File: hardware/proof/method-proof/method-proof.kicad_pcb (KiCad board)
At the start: 4 copper layers, 40 x 30 mm, 21 parts, among them J1 5V_IN, J2 OUT, J3 PA1, U1 MCP1700T-3302E/TT, U2 MSPS003F4SPW20R

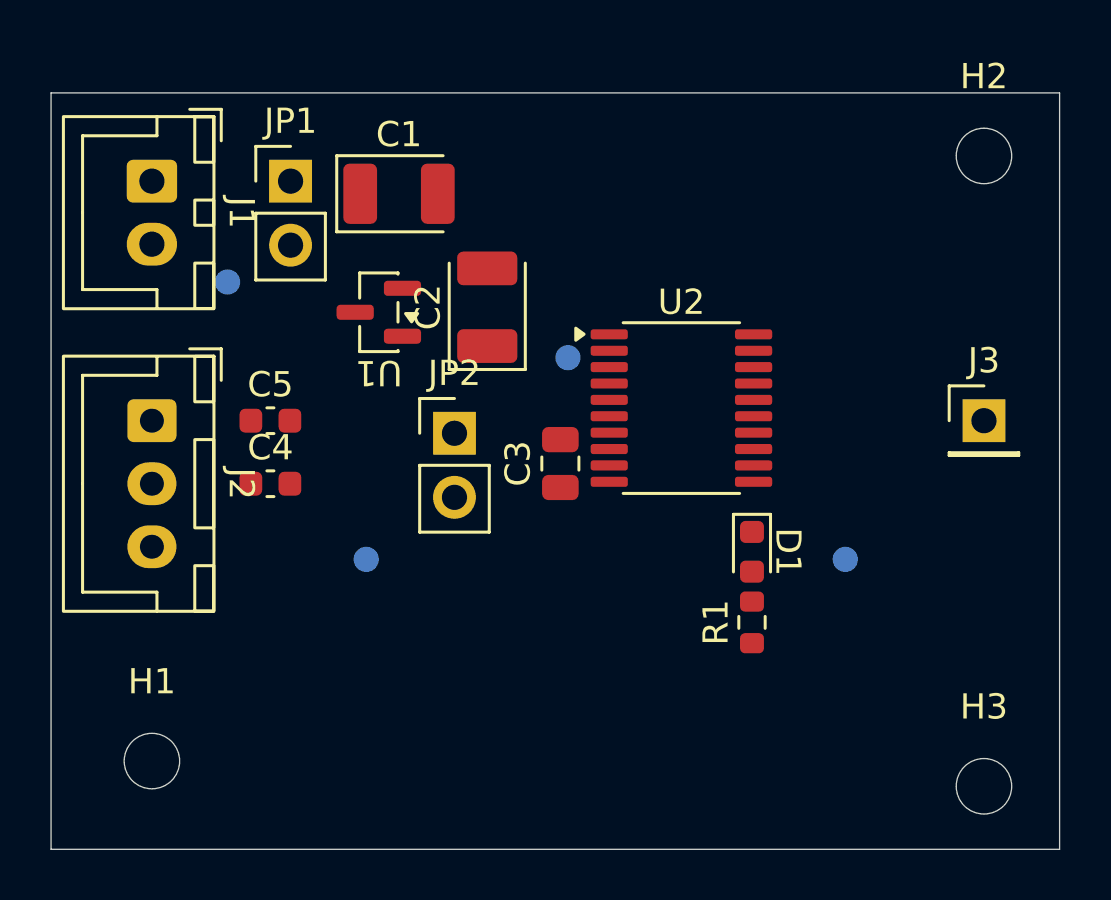
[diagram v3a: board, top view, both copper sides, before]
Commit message: hardware(method-proof): placement candidate 3: candidate 1 with the controller and the LED stage moved down four millimetres and the PA1 header with them
Not for manufacture.

Co-Authored-By: Claude Sonnet 5.5 <noreply@anthropic.com>
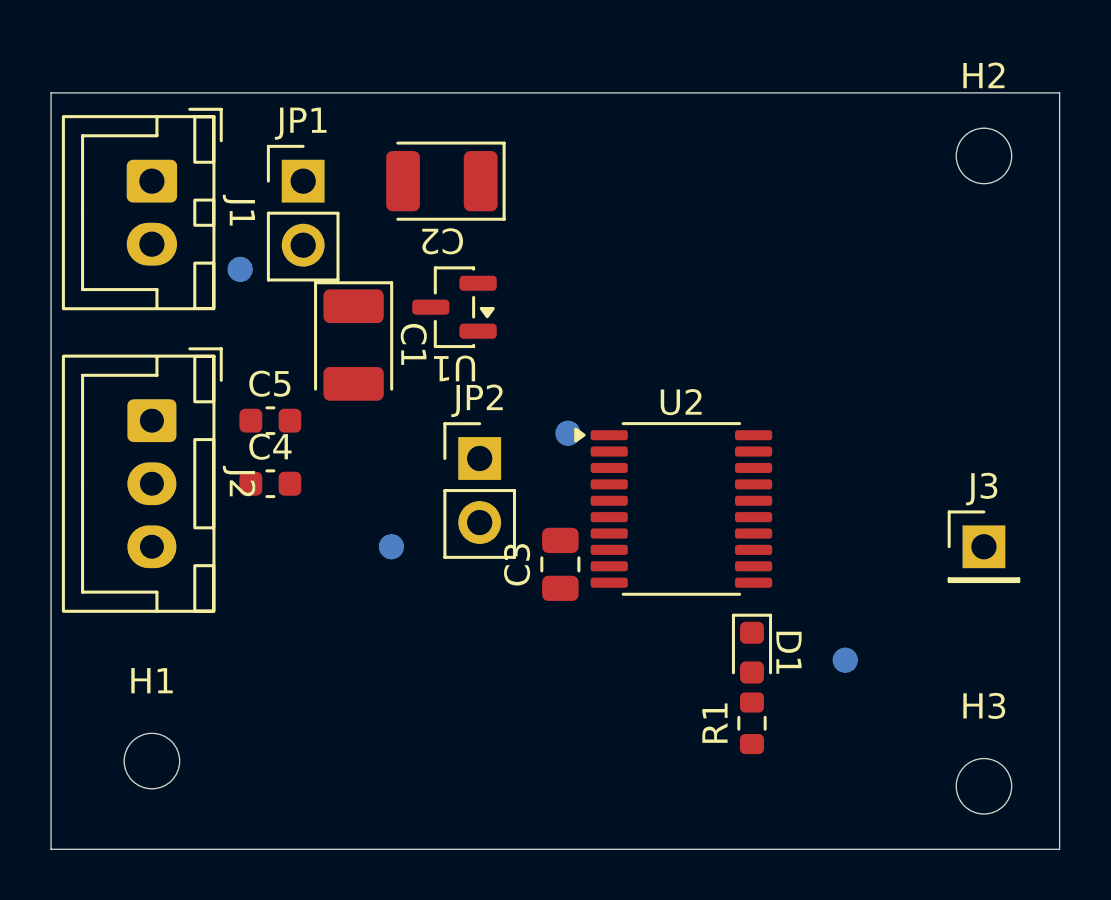
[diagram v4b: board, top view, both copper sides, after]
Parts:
- moved C1 6.26 mm to (112.0, 110.0), turned to -90 degrees
- moved C2 5.31 mm to (115.5, 103.5), turned to 180 degrees
- moved J3 5.00 mm to (137.0, 118.0)
- moved C3 4.00 mm to (120.2, 118.7)
- moved D1 4.00 mm to (127.8, 122.2)
- moved R1 4.00 mm to (127.8, 125.0)
- moved TP4 4.00 mm to (131.5, 122.5)
- moved U2 4.00 mm to (125.0, 116.5)
- moved U1 3.01 mm to (116.0, 108.5)
- moved TP3 3.00 mm to (120.5, 113.5)
- moved JP2 1.41 mm to (117.0, 114.5)
- moved TP2 1.12 mm to (113.5, 118.0)
- moved TP1 0.71 mm to (107.5, 107.0)
- moved JP1 0.50 mm to (110.0, 103.5)
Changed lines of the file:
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@@
 	(footprint "Connector_PinHeader_2.54mm:PinHeader_1x01_P2.54mm_Vertical"
 		(layer "F.Cu")
-		(at 137 113)
+		(at 137 118)
 		(property "Reference" "J3"
 			(at 0 -2.38 0)
@@
 	(footprint "Package_SO:TSSOP-20_4.4x6.5mm_P0.65mm"
 		(layer "F.Cu")
-		(at 125 112.5)
+		(at 125 116.5)
 		(property "Reference" "U2"
 			(at 0 -4.2 0)
@@
 	(footprint "Connector_PinHeader_2.54mm:PinHeader_1x02_P2.54mm_Vertical"
 		(layer "F.Cu")
-		(at 109.5 103.5)
+		(at 110 103.5)
 		(property "Reference" "JP1"
 			(at 0 -2.38 0)
@@
 	(footprint "Resistor_SMD:R_0603_1608Metric"
 		(layer "F.Cu")
-		(at 127.8 121 90)
+		(at 127.8 125 90)
 		(property "Reference" "R1"
 			(at 0 -1.43 90)
@@
 	(footprint "Capacitor_Tantalum_SMD:CP_EIA-3528-21_Kemet-B"
 		(layer "F.Cu")
-		(at 113.8 104)
+		(at 112 110 -90)
 		(property "Reference" "C1"
-			(at 0 -2.35 0)
+			(at 0 -2.35 270)
 			(unlocked yes)
 			(layer "F.SilkS")
@@
 		)
 		(property "Value" "47uF"
-			(at 0 2.35 0)
+			(at 0 2.35 270)
 			(unlocked yes)
 			(layer "F.SilkS")
@@
 		)
 		(property "Datasheet" ""
-			(at 0 0 0)
+			(at 0 0 270)
 			(layer "F.Fab")
 			(hide yes)
@@
 		)
 		(property "Description" ""
-			(at 0 0 0)
+			(at 0 0 270)
 			(layer "F.Fab")
 			(hide yes)
@@
 		(duplicate_pad_numbers_are_jumpers no)
 		(fp_line
-			(start -2.470001 -1.510001)
-			(end -2.470001 1.51)
+			(start -2.470001 1.51)
+			(end 1.75 1.51)
 			(stroke
 				(width 0.12)
@@
 		)
 		(fp_line
-			(start -2.470001 1.51)
-			(end 1.75 1.51)
+			(start -2.470001 -1.510001)
+			(end -2.470001 1.51)
 			(stroke
 				(width 0.12)
@@
 		)
 		(fp_line
-			(start -1.75 -0.7)
-			(end -1.75 1.4)
+			(start -1.75 1.4)
+			(end 1.75 1.4)
 			(stroke
 				(width 0.1)
@@
 		)
 		(fp_line
-			(start -1.75 1.4)
-			(end 1.75 1.4)
+			(start 1.75 1.4)
+			(end 1.75 -1.4)
 			(stroke
 				(width 0.1)
@@
 		)
 		(fp_line
-			(start -1.05 -1.4)
-			(end -1.75 -0.7)
+			(start -1.75 -0.7)
+			(end -1.75 1.4)
 			(stroke
 				(width 0.1)
@@
 		)
 		(fp_line
-			(start 1.75 -1.4)
-			(end -1.05 -1.4)
+			(start -1.05 -1.4)
+			(end -1.75 -0.7)
 			(stroke
 				(width 0.1)
@@
 		)
 		(fp_line
-			(start 1.75 1.4)
-			(end 1.75 -1.4)
+			(start 1.75 -1.4)
+			(end -1.05 -1.4)
 			(stroke
 				(width 0.1)
@@
 		)
 		(fp_text user "${REFERENCE}"
-			(at 0 0 0)
+			(at 0 0 270)
 			(unlocked yes)
 			(layer "F.Fab")
@@
 		)
 		(pad "1" smd roundrect
-			(at -1.54 0)
+			(at -1.54 0 270)
 			(size 1.34 2.39)
 			(layers "F.Cu" "F.Mask" "F.Paste")
@@
 		)
 		(pad "2" smd roundrect
-			(at 1.539999 0)
+			(at 1.539999 0 270)
 			(size 1.34 2.39)
 			(layers "F.Cu" "F.Mask" "F.Paste")
@@
 	(footprint "Package_TO_SOT_SMD:SOT-23"
 		(layer "F.Cu")
-		(at 113 108.7 180)
+		(at 116 108.5 180)
 		(property "Reference" "U1"
 			(at 0 -2.4 180)
@@
 	(footprint "Capacitor_Tantalum_SMD:CP_EIA-3528-21_Kemet-B"
 		(layer "F.Cu")
-		(at 117.3 108.5 90)
+		(at 115.5 103.5 180)
 		(property "Reference" "C2"
-			(at 0 -2.35 90)
+			(at 0 -2.35 180)
 			(unlocked yes)
 			(layer "F.SilkS")
@@
 		)
 		(property "Value" "150uF"
-			(at 0 2.35 90)
+			(at 0 2.35 180)
 			(unlocked yes)
 			(layer "F.SilkS")
@@
 		)
 		(property "Datasheet" ""
-			(at 0 0 90)
+			(at 0 0 180)
 			(layer "F.Fab")
 			(hide yes)
@@
 		)
 		(property "Description" ""
-			(at 0 0 90)
+			(at 0 0 180)
 			(layer "F.Fab")
 			(hide yes)
@@
 		)
 		(fp_line
-			(start -2.470001 -1.51)
-			(end -2.470001 1.51)
+			(start -2.470001 1.51)
+			(end 1.75 1.51)
 			(stroke
 				(width 0.12)
@@
 		)
 		(fp_line
-			(start -2.470001 1.51)
-			(end 1.75 1.51)
+			(start -2.470001 -1.51)
+			(end -2.470001 1.51)
 			(stroke
 				(width 0.12)
@@
 		)
 		(fp_line
-			(start 1.75 -1.4)
-			(end -1.05 -1.4)
+			(start 1.75 1.4)
+			(end 1.75 -1.4)
 			(stroke
 				(width 0.1)
@@
 		)
 		(fp_line
-			(start -1.05 -1.4)
-			(end -1.75 -0.7)
+			(start 1.75 -1.4)
+			(end -1.05 -1.4)
 			(stroke
 				(width 0.1)
@@
 		)
 		(fp_line
-			(start -1.75 -0.7)
-			(end -1.75 1.4)
+			(start -1.05 -1.4)
+			(end -1.75 -0.7)
 			(stroke
 				(width 0.1)
@@
 		)
 		(fp_line
-			(start 1.75 1.4)
-			(end 1.75 -1.4)
+			(start -1.75 1.4)
+			(end 1.75 1.4)
 			(stroke
 				(width 0.1)
@@
 		)
 		(fp_line
-			(start -1.75 1.4)
-			(end 1.75 1.4)
+			(start -1.75 -0.7)
+			(end -1.75 1.4)
 			(stroke
 				(width 0.1)
@@
 		)
 		(fp_text user "${REFERENCE}"
-			(at 0 0 90)
+			(at 0 0 180)
 			(unlocked yes)
 			(layer "F.Fab")
@@
 		)
 		(pad "1" smd roundrect
-			(at -1.54 0 90)
+			(at -1.54 0 180)
 			(size 1.34 2.39)
 			(layers "F.Cu" "F.Mask" "F.Paste")
@@
 		)
 		(pad "2" smd roundrect
-			(at 1.539999 0 90)
+			(at 1.539999 0 180)
 			(size 1.34 2.39)
 			(layers "F.Cu" "F.Mask" "F.Paste")
@@
 	(footprint "Capacitor_SMD:C_0805_2012Metric"
 		(layer "F.Cu")
-		(at 120.2 114.7 90)
+		(at 120.2 118.7 90)
 		(property "Reference" "C3"
 			(at 0 -1.68 90)
@@
 	(footprint "LED_SMD:LED_0603_1608Metric"
 		(layer "F.Cu")
-		(at 127.8 118.2 -90)
+		(at 127.8 122.2 -90)
 		(property "Reference" "D1"
-			(at 0 -1.43 270)
+			(at 0 -1.43 -90)
 			(unlocked yes)
 			(layer "F.SilkS")
@@
 		)
 		(property "Value" "VLMG1300-GS08"
-			(at 0 1.43 270)
+			(at 0 1.43 -90)
 			(unlocked yes)
 			(layer "F.SilkS")
@@
 		)
 		(property "Datasheet" ""
-			(at 0 0 270)
+			(at 0 0 -90)
 			(layer "F.Fab")
 			(hide yes)
@@
 		)
 		(property "Description" ""
-			(at 0 0 270)
+			(at 0 0 -90)
 			(layer "F.Fab")
 			(hide yes)
@@
 		)
 		(fp_text user "${REFERENCE}"
-			(at 0 0 270)
+			(at 0 0 -90)
 			(unlocked yes)
 			(layer "F.Fab")
@@
 	(footprint "Connector_PinHeader_2.54mm:PinHeader_1x02_P2.54mm_Vertical"
 		(layer "F.Cu")
-		(at 116 113.5)
+		(at 117 114.5)
 		(property "Reference" "JP2"
 			(at 0 -2.38 0)
@@
 	(footprint "TestPoint:TestPoint_Pad_D1.0mm"
 		(layer "B.Cu")
-		(at 120.5 110.5)
+		(at 120.5 113.5)
 		(property "Reference" "TP3"
 			(at 0 1.448 180)
@@
 	(footprint "TestPoint:TestPoint_Pad_D1.0mm"
 		(layer "B.Cu")
-		(at 107 107.5)
+		(at 107.5 107)
 		(property "Reference" "TP1"
 			(at 0 1.448 180)
@@
 	(footprint "TestPoint:TestPoint_Pad_D1.0mm"
 		(layer "B.Cu")
-		(at 131.5 118.5)
+		(at 131.5 122.5)
 		(property "Reference" "TP4"
 			(at 0 1.448 180)
@@
 	(footprint "TestPoint:TestPoint_Pad_D1.0mm"
 		(layer "B.Cu")
-		(at 112.5 118.5)
+		(at 113.5 118)
 		(property "Reference" "TP2"
 			(at 0 1.448 180)

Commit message: hardware(method-proof): placement candidate 4: candidate 1 with the controller, the LED stage and C1 moved clear of their neighbours' courtyards
Not for manufacture. The first three candidates each leave courtyards overlapping
(U2 with C3, R1 with D1 and, in two of them, JP1 with C1); candidate 4 moves
U2 0.8 mm right, D1 and R1 0.8 mm right and apart, and C1 1 mm down, and
leaves none.

Co-Authored-By: Claude Sonnet 5.5 <noreply@anthropic.com>
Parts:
- moved J3 5.00 mm to (137.0, 113.0)
- moved D1 4.08 mm to (128.6, 118.2)
- moved U2 4.08 mm to (125.8, 112.5)
- moved TP4 4.06 mm to (132.2, 118.5)
- moved C3 4.00 mm to (120.2, 114.7)
- moved R1 3.49 mm to (128.6, 121.6)
- moved TP3 3.00 mm to (120.5, 110.5)
- moved C1 1.00 mm to (112.0, 111.0)
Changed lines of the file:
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@@
 	(footprint "Connector_PinHeader_2.54mm:PinHeader_1x01_P2.54mm_Vertical"
 		(layer "F.Cu")
-		(at 137 118)
+		(at 137 113)
 		(property "Reference" "J3"
 			(at 0 -2.38 0)
@@
 	(footprint "Package_SO:TSSOP-20_4.4x6.5mm_P0.65mm"
 		(layer "F.Cu")
-		(at 125 116.5)
+		(at 125.8 112.5)
 		(property "Reference" "U2"
 			(at 0 -4.2 0)
@@
 	(footprint "Resistor_SMD:R_0603_1608Metric"
 		(layer "F.Cu")
-		(at 127.8 125 90)
+		(at 128.6 121.6 90)
 		(property "Reference" "R1"
 			(at 0 -1.43 90)
@@
 	(footprint "Capacitor_Tantalum_SMD:CP_EIA-3528-21_Kemet-B"
 		(layer "F.Cu")
-		(at 112 110 -90)
+		(at 112 111 -90)
 		(property "Reference" "C1"
-			(at 0 -2.35 270)
+			(at 0 -2.35 -90)
 			(unlocked yes)
 			(layer "F.SilkS")
@@
 		)
 		(property "Value" "47uF"
-			(at 0 2.35 270)
+			(at 0 2.35 -90)
 			(unlocked yes)
 			(layer "F.SilkS")
@@
 		)
 		(property "Datasheet" ""
-			(at 0 0 270)
+			(at 0 0 -90)
 			(layer "F.Fab")
 			(hide yes)
@@
 		)
 		(property "Description" ""
-			(at 0 0 270)
+			(at 0 0 -90)
 			(layer "F.Fab")
 			(hide yes)
@@
 		)
 		(fp_text user "${REFERENCE}"
-			(at 0 0 270)
+			(at 0 0 -90)
 			(unlocked yes)
 			(layer "F.Fab")
@@
 	(footprint "Capacitor_SMD:C_0805_2012Metric"
 		(layer "F.Cu")
-		(at 120.2 118.7 90)
+		(at 120.2 114.7 90)
 		(property "Reference" "C3"
 			(at 0 -1.68 90)
@@
 	(footprint "LED_SMD:LED_0603_1608Metric"
 		(layer "F.Cu")
-		(at 127.8 122.2 -90)
+		(at 128.6 118.2 -90)
 		(property "Reference" "D1"
 			(at 0 -1.43 -90)
@@
 	(footprint "TestPoint:TestPoint_Pad_D1.0mm"
 		(layer "B.Cu")
-		(at 120.5 113.5)
+		(at 120.5 110.5)
 		(property "Reference" "TP3"
 			(at 0 1.448 180)
@@
 	(footprint "TestPoint:TestPoint_Pad_D1.0mm"
 		(layer "B.Cu")
-		(at 131.5 122.5)
+		(at 132.199999 118.5)
 		(property "Reference" "TP4"
 			(at 0 1.448 180)

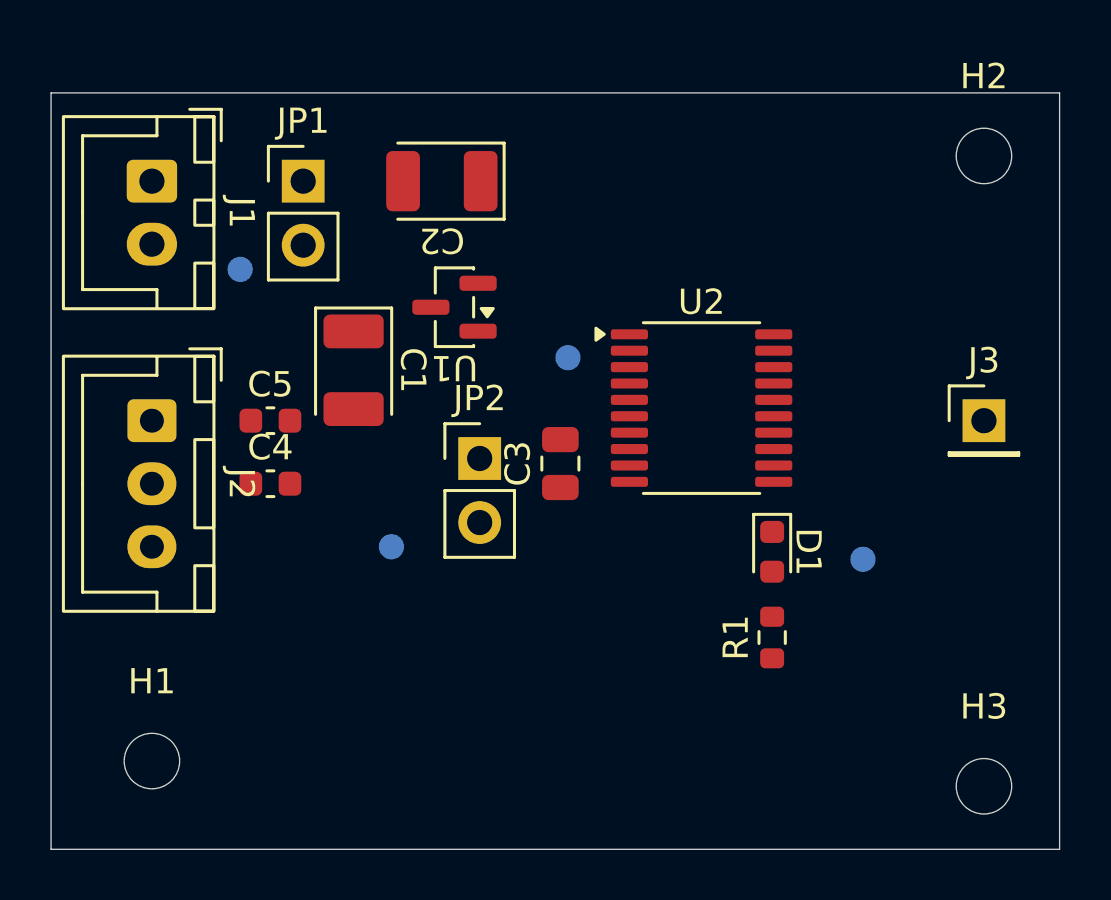
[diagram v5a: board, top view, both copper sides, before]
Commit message: hardware(method-proof): placement candidate 5: candidate 4 with the first link moved right and the regulator's output capacitor stood up, so TP1 and TP2 clear the tall parts
Not for manufacture. JP1 moves 3 mm right and TP1 into the gap it leaves beside J1,
C2 stands up above U1, U1 moves 1 mm down and TP2 1 mm left; no courtyards overlap
and every test point stands 2 mm or more from a part taller than 2.6 mm.

Co-Authored-By: Claude Sonnet 5.5 <noreply@anthropic.com>
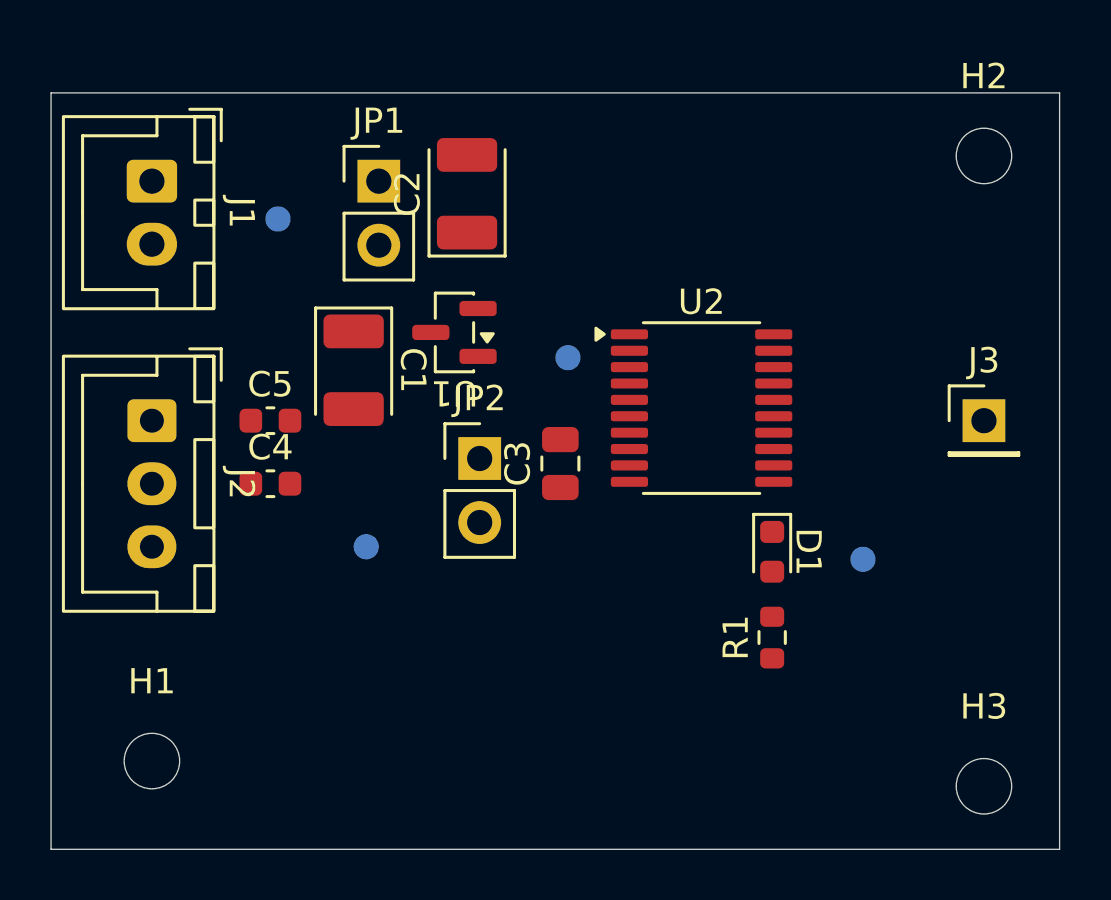
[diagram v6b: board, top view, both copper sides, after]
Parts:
- moved JP1 3.00 mm to (113.0, 103.5)
- moved TP1 2.50 mm to (109.0, 105.0)
- moved C2 1.12 mm to (116.5, 104.0), turned to 90 degrees
- moved TP2 1.00 mm to (112.5, 118.0)
- moved U1 1.00 mm to (116.0, 109.5)
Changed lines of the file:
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@@
 	(footprint "Connector_PinHeader_2.54mm:PinHeader_1x02_P2.54mm_Vertical"
 		(layer "F.Cu")
-		(at 110 103.5)
+		(at 113 103.5)
 		(property "Reference" "JP1"
 			(at 0 -2.38 0)
@@
 		(at 112 111 -90)
 		(property "Reference" "C1"
-			(at 0 -2.35 -90)
+			(at 0 -2.35 270)
 			(unlocked yes)
 			(layer "F.SilkS")
@@
 		)
 		(property "Value" "47uF"
-			(at 0 2.35 -90)
+			(at 0 2.35 270)
 			(unlocked yes)
 			(layer "F.SilkS")
@@
 		)
 		(property "Datasheet" ""
-			(at 0 0 -90)
+			(at 0 0 270)
 			(layer "F.Fab")
 			(hide yes)
@@
 		)
 		(property "Description" ""
-			(at 0 0 -90)
+			(at 0 0 270)
 			(layer "F.Fab")
 			(hide yes)
@@
 		)
 		(fp_text user "${REFERENCE}"
-			(at 0 0 -90)
+			(at 0 0 270)
 			(unlocked yes)
 			(layer "F.Fab")
@@
 	(footprint "Package_TO_SOT_SMD:SOT-23"
 		(layer "F.Cu")
-		(at 116 108.5 180)
+		(at 116 109.5 180)
 		(property "Reference" "U1"
 			(at 0 -2.4 180)
@@
 	(footprint "Capacitor_Tantalum_SMD:CP_EIA-3528-21_Kemet-B"
 		(layer "F.Cu")
-		(at 115.5 103.5 180)
+		(at 116.5 104 90)
 		(property "Reference" "C2"
-			(at 0 -2.35 180)
+			(at 0 -2.35 90)
 			(unlocked yes)
 			(layer "F.SilkS")
@@
 		)
 		(property "Value" "150uF"
-			(at 0 2.35 180)
+			(at 0 2.35 90)
 			(unlocked yes)
 			(layer "F.SilkS")
@@
 		)
 		(property "Datasheet" ""
-			(at 0 0 180)
+			(at 0 0 90)
 			(layer "F.Fab")
 			(hide yes)
@@
 		)
 		(property "Description" ""
-			(at 0 0 180)
+			(at 0 0 90)
 			(layer "F.Fab")
 			(hide yes)
@@
 		)
 		(fp_line
+			(start -2.470001 -1.51)
+			(end -2.470001 1.51)
+			(stroke
+				(width 0.12)
+				(type default)
+			)
+			(layer "F.SilkS")
+		)
+		(fp_line
 			(start -2.470001 1.51)
 			(end 1.75 1.51)
-			(stroke
-				(width 0.12)
-				(type default)
-			)
-			(layer "F.SilkS")
-		)
-		(fp_line
-			(start -2.470001 -1.51)
-			(end -2.470001 1.51)
 			(stroke
 				(width 0.12)
@@
 		)
 		(fp_line
+			(start 1.75 -1.4)
+			(end -1.05 -1.4)
+			(stroke
+				(width 0.1)
+				(type default)
+			)
+			(layer "F.Fab")
+		)
+		(fp_line
+			(start -1.05 -1.4)
+			(end -1.75 -0.7)
+			(stroke
+				(width 0.1)
+				(type default)
+			)
+			(layer "F.Fab")
+		)
+		(fp_line
+			(start -1.75 -0.7)
+			(end -1.75 1.4)
+			(stroke
+				(width 0.1)
+				(type default)
+			)
+			(layer "F.Fab")
+		)
+		(fp_line
 			(start 1.75 1.4)
 			(end 1.75 -1.4)
@@
 		)
 		(fp_line
-			(start 1.75 -1.4)
-			(end -1.05 -1.4)
-			(stroke
-				(width 0.1)
-				(type default)
-			)
-			(layer "F.Fab")
-		)
-		(fp_line
-			(start -1.05 -1.4)
-			(end -1.75 -0.7)
-			(stroke
-				(width 0.1)
-				(type default)
-			)
-			(layer "F.Fab")
-		)
-		(fp_line
 			(start -1.75 1.4)
 			(end 1.75 1.4)
@@
 			(layer "F.Fab")
 		)
-		(fp_line
-			(start -1.75 -0.7)
-			(end -1.75 1.4)
-			(stroke
-				(width 0.1)
-				(type default)
-			)
-			(layer "F.Fab")
-		)
 		(fp_text user "${REFERENCE}"
-			(at 0 0 180)
+			(at 0 0 90)
 			(unlocked yes)
 			(layer "F.Fab")
@@
 		)
 		(pad "1" smd roundrect
-			(at -1.54 0 180)
+			(at -1.54 0 90)
 			(size 1.34 2.39)
 			(layers "F.Cu" "F.Mask" "F.Paste")
@@
 		)
 		(pad "2" smd roundrect
-			(at 1.539999 0 180)
+			(at 1.539999 0 90)
 			(size 1.34 2.39)
 			(layers "F.Cu" "F.Mask" "F.Paste")
@@
 		(at 128.6 118.2 -90)
 		(property "Reference" "D1"
-			(at 0 -1.43 -90)
+			(at 0 -1.43 270)
 			(unlocked yes)
 			(layer "F.SilkS")
@@
 		)
 		(property "Value" "VLMG1300-GS08"
-			(at 0 1.43 -90)
+			(at 0 1.43 270)
 			(unlocked yes)
 			(layer "F.SilkS")
@@
 		)
 		(property "Datasheet" ""
-			(at 0 0 -90)
+			(at 0 0 270)
 			(layer "F.Fab")
 			(hide yes)
@@
 		)
 		(property "Description" ""
-			(at 0 0 -90)
+			(at 0 0 270)
 			(layer "F.Fab")
 			(hide yes)
@@
 		)
 		(fp_text user "${REFERENCE}"
-			(at 0 0 -90)
+			(at 0 0 270)
 			(unlocked yes)
 			(layer "F.Fab")
@@
 	(footprint "TestPoint:TestPoint_Pad_D1.0mm"
 		(layer "B.Cu")
-		(at 107.5 107)
+		(at 109 105)
 		(property "Reference" "TP1"
 			(at 0 1.448 180)
@@
 	(footprint "TestPoint:TestPoint_Pad_D1.0mm"
 		(layer "B.Cu")
-		(at 113.5 118)
+		(at 112.5 118)
 		(property "Reference" "TP2"
 			(at 0 1.448 180)
